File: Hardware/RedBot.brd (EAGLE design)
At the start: 94 x 49.5 mm, 63 parts, among them U1 ATMEGA328P, U2 TB6612FNG, U3 MIC5219 5V, U4 MIC5219 3.3V, U5 FT232RLSSOP, U6 7408SE, Y1 16MHz

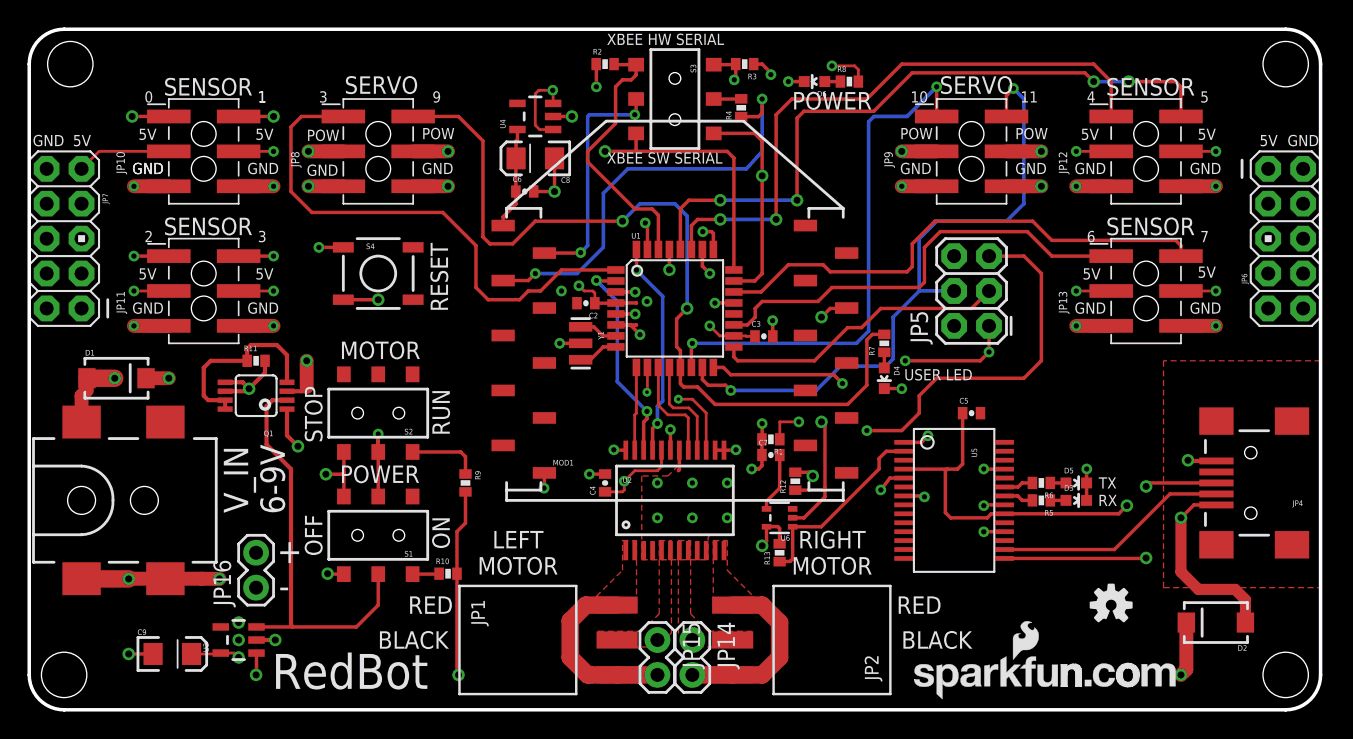
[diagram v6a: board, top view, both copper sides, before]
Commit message: V03 prototypes - Added an AND gate instead of two diodes for reset control - Changed packages on the 5x2 headers along the board edges to be no silk - Moved motor header text to avoid tmask interference - Added bypass cap to FTDI chip - Grounded test pin on FTDI chip
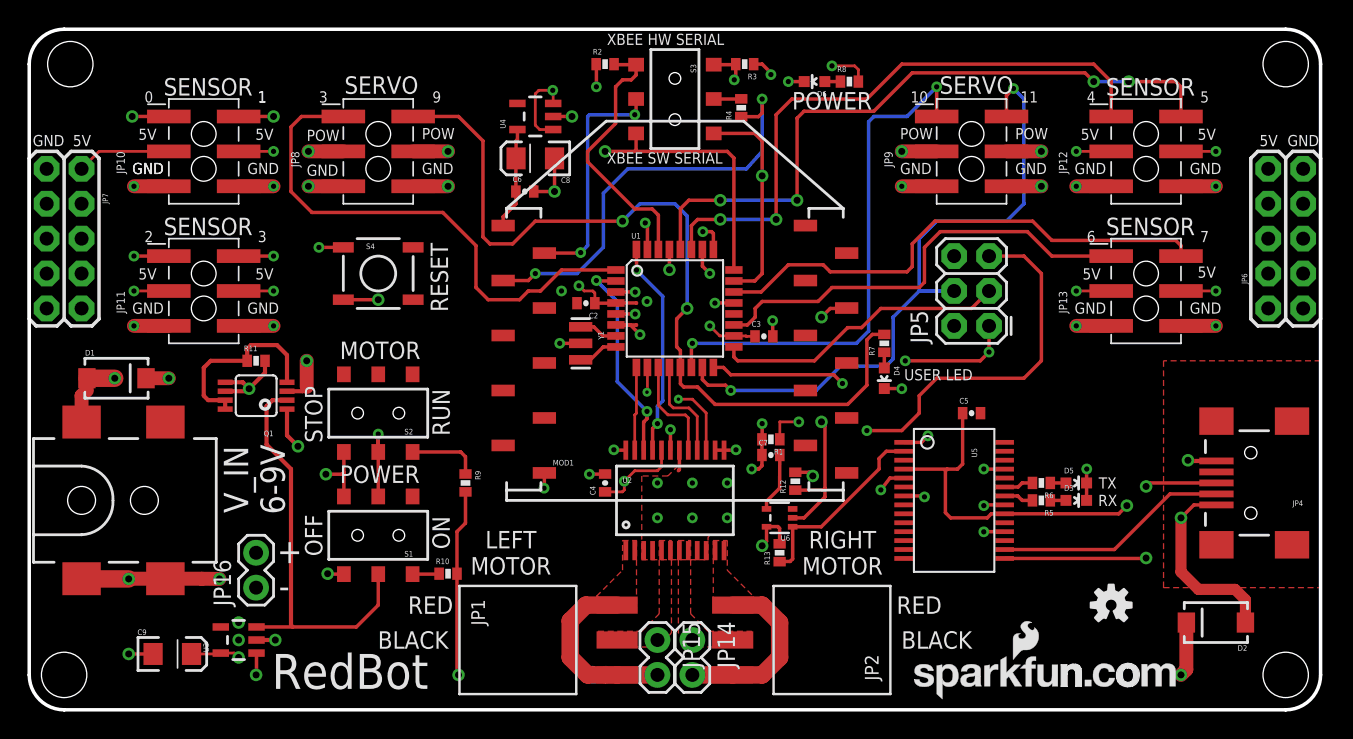
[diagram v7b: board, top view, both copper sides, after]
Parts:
- JP6, JP7: value M05X2PTH -> M05X2NO_SILK; device SparkFun-Connectors:AVR_ICSP -> SparkFun-Connectors:2X5_NOSILK
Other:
- board text added: "v03"
- board text removed: "v10"
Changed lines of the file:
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@@
 <grid distance="0.05" unitdist="inch" unit="inch" style="lines" multiple="1" display="yes" altdistance="0.005" altunitdist="inch" altunit="inch"/>
 <layers>
-<layer number="1" name="Top" color="4" fill="1" visible="yes" active="yes"/>
-<layer number="2" name="5V" color="1" fill="3" visible="yes" active="yes"/>
-<layer number="15" name="Gnd" color="4" fill="6" visible="yes" active="yes"/>
+<layer number="1" name="Top" color="4" fill="1" visible="no" active="yes"/>
+<layer number="2" name="5V" color="1" fill="3" visible="no" active="yes"/>
+<layer number="15" name="Gnd" color="4" fill="6" visible="no" active="yes"/>
 <layer number="16" name="Bottom" color="1" fill="1" visible="yes" active="yes"/>
 <layer number="17" name="Pads" color="2" fill="1" visible="yes" active="yes"/>
@@
 <layer number="19" name="Unrouted" color="6" fill="1" visible="yes" active="yes"/>
 <layer number="20" name="Dimension" color="15" fill="1" visible="yes" active="yes"/>
-<layer number="21" name="tPlace" color="16" fill="1" visible="yes" active="yes"/>
+<layer number="21" name="tPlace" color="16" fill="1" visible="no" active="yes"/>
 <layer number="22" name="bPlace" color="14" fill="1" visible="yes" active="yes"/>
-<layer number="23" name="tOrigins" color="15" fill="1" visible="yes" active="yes"/>
+<layer number="23" name="tOrigins" color="15" fill="1" visible="no" active="yes"/>
 <layer number="24" name="bOrigins" color="15" fill="1" visible="yes" active="yes"/>
 <layer number="25" name="tNames" color="7" fill="1" visible="no" active="yes"/>
@@
 <layer number="42" name="bRestrict" color="1" fill="10" visible="no" active="yes"/>
 <layer number="44" name="Drills" color="7" fill="1" visible="no" active="yes"/>
-<layer number="45" name="Holes" color="7" fill="1" visible="yes" active="yes"/>
+<layer number="45" name="Holes" color="7" fill="1" visible="no" active="yes"/>
 <layer number="46" name="Milling" color="3" fill="1" visible="no" active="yes"/>
-<layer number="51" name="tDocu" color="6" fill="1" visible="yes" active="yes"/>
+<layer number="51" name="tDocu" color="6" fill="1" visible="no" active="yes"/>
 <layer number="52" name="bDocu" color="7" fill="1" visible="no" active="yes"/>
 <layer number="3" name="Route3" color="4" fill="3" visible="no" active="no"/>
@@
 <text x="78.486" y="16.51" size="0.8128" layer="21" font="vector" ratio="15" align="center">TX</text>
 <text x="78.486" y="15.24" size="0.8128" layer="21" font="vector" ratio="15" align="center">RX</text>
-<text x="35.56" y="11.43" size="1.27" layer="21" font="vector" ratio="15" align="center">LEFT
+<text x="35.052" y="11.43" size="1.27" layer="21" font="vector" ratio="15" align="center">LEFT
 MOTOR</text>
-<text x="58.42" y="11.43" size="1.27" layer="21" font="vector" ratio="15" align="center">RIGHT
+<text x="59.182" y="11.43" size="1.27" layer="21" font="vector" ratio="15" align="center">RIGHT
 MOTOR</text>
 <text x="64.77" y="7.62" size="1.27" layer="21" font="vector" ratio="15" align="center">RED</text>
@@
 <text x="58.42" y="44.323" size="1.27" layer="21" font="vector" ratio="15" align="center">POWER</text>
 <text x="66.167" y="24.384" size="0.8128" layer="21" font="vector" ratio="15" align="center">USER LED</text>
-<text x="41.91" y="2.54" size="1.27" layer="16" font="vector" ratio="15" rot="MR0" align="center">v10</text>
+<text x="41.91" y="2.54" size="1.27" layer="16" font="vector" ratio="15" rot="MR0" align="center">v03</text>
 <text x="3.175" y="41.021" size="0.8128" layer="21" font="vector" ratio="15">5V</text>
 <text x="7.493" y="38.989" size="0.8128" layer="21" font="vector" ratio="15">GND</text>
@@
 <text x="18.034" y="10.668" size="1.778" layer="21" font="vector" ratio="15">+</text>
 <text x="18.161" y="8.128" size="1.778" layer="21" font="vector" ratio="15">-</text>
+<wire x1="2.54" y1="40.132" x2="3.048" y2="40.64" width="0.254" layer="21"/>
+<wire x1="3.048" y1="40.64" x2="4.572" y2="40.64" width="0.254" layer="21"/>
+<wire x1="4.572" y1="40.64" x2="5.08" y2="40.132" width="0.254" layer="21"/>
+<wire x1="5.08" y1="40.132" x2="5.08" y2="28.448" width="0.254" layer="21"/>
+<wire x1="5.08" y1="28.448" x2="4.572" y2="27.94" width="0.254" layer="21"/>
+<wire x1="4.572" y1="27.94" x2="3.048" y2="27.94" width="0.254" layer="21"/>
+<wire x1="3.048" y1="27.94" x2="2.54" y2="28.448" width="0.254" layer="21"/>
+<wire x1="2.54" y1="28.448" x2="2.54" y2="40.132" width="0.254" layer="21"/>
+<wire x1="2.54" y1="40.132" x2="2.032" y2="40.64" width="0.254" layer="21"/>
+<wire x1="2.032" y1="40.64" x2="0.508" y2="40.64" width="0.254" layer="21"/>
+<wire x1="0.508" y1="40.64" x2="0" y2="40.132" width="0.254" layer="21"/>
+<wire x1="0" y1="40.132" x2="0" y2="28.448" width="0.254" layer="21"/>
+<wire x1="0" y1="28.448" x2="0.508" y2="27.94" width="0.254" layer="21"/>
+<wire x1="0.508" y1="27.94" x2="2.032" y2="27.94" width="0.254" layer="21"/>
+<wire x1="2.032" y1="27.94" x2="2.54" y2="28.448" width="0.254" layer="21"/>
+<wire x1="91.44" y1="40.132" x2="91.948" y2="40.64" width="0.254" layer="21"/>
+<wire x1="91.948" y1="40.64" x2="93.472" y2="40.64" width="0.254" layer="21"/>
+<wire x1="93.472" y1="40.64" x2="93.98" y2="40.132" width="0.254" layer="21"/>
+<wire x1="93.98" y1="40.132" x2="93.98" y2="28.448" width="0.254" layer="21"/>
+<wire x1="93.98" y1="28.448" x2="93.472" y2="27.94" width="0.254" layer="21"/>
+<wire x1="93.472" y1="27.94" x2="91.948" y2="27.94" width="0.254" layer="21"/>
+<wire x1="91.948" y1="27.94" x2="91.44" y2="28.448" width="0.254" layer="21"/>
+<wire x1="91.44" y1="28.448" x2="91.44" y2="40.132" width="0.254" layer="21"/>
+<wire x1="91.44" y1="40.132" x2="90.932" y2="40.64" width="0.254" layer="21"/>
+<wire x1="90.932" y1="40.64" x2="89.408" y2="40.64" width="0.254" layer="21"/>
+<wire x1="89.408" y1="40.64" x2="88.9" y2="40.132" width="0.254" layer="21"/>
+<wire x1="88.9" y1="40.132" x2="88.9" y2="28.448" width="0.254" layer="21"/>
+<wire x1="88.9" y1="28.448" x2="89.408" y2="27.94" width="0.254" layer="21"/>
+<wire x1="89.408" y1="27.94" x2="90.932" y2="27.94" width="0.254" layer="21"/>
+<wire x1="90.932" y1="27.94" x2="91.44" y2="28.448" width="0.254" layer="21"/>
 </plain>
 <attributes>
@@
 <attribute name="VALUE" value="1k" x="51.816" y="43.815" size="1.778" layer="27" font="vector" ratio="15" rot="R90" display="off"/>
 </element>
-<element name="JP6" library="SparkFun-Connectors" package="AVR_ICSP" value="M05X2PTH" x="91.44" y="34.29"/>
-<element name="JP7" library="SparkFun-Connectors" package="AVR_ICSP" value="M05X2PTH" x="2.54" y="34.29" rot="R180"/>
+<element name="JP6" library="SparkFun-Connectors" package="2X5_NOSILK" value="M05X2NO_SILK" x="91.44" y="34.29"/>
+<element name="JP7" library="SparkFun-Connectors" package="2X5_NOSILK" value="M05X2NO_SILK" x="2.54" y="34.29" rot="R180"/>
 <element name="U$17" library="SparkFun-Aesthetics" package="OSHW-LOGO-S" value="OSHW-LOGOS" x="78.74" y="7.62"/>
 <element name="SFE-LOGO1" library="SparkFun-Aesthetics" package="SFE-NEW-WEBLOGO" value="LOGO-SFENEW" x="64.389" y="0.762"/>
@@
 </element>
 <element name="JP16" library="SparkFun-Connectors" package="1X02" value="" x="16.51" y="8.89" rot="R90"/>
-<element name="U6" library="SparkFun-DigitalIC" package="SOT353" value="7408SE" x="54.61" y="13.97" rot="R90"/>
+<element name="U6" library="SparkFun-DigitalIC" package="SOT353" value="7408SE" x="54.61" y="13.97" rot="R90">
+<attribute name="PROD_ID" value="IC-10841" x="54.61" y="13.97" size="1.778" layer="27" rot="R90" display="off"/>
+<attribute name="VALUE" value="74LVC1G08SE-7" x="54.61" y="13.97" size="1.778" layer="27" rot="R90" display="off"/>
+</element>
 <element name="R12" library="SparkFun-Resistors" package="0402-RES" value="10k" x="55.753" y="16.637" rot="R90">
 <attribute name="PROD_ID" value="RES-00824" x="55.753" y="16.637" size="1.778" layer="27" font="vector" ratio="15" rot="R90" display="off"/>
@@
 </signal>
 </signals>
-<errors>
-</errors>
 </board>
 </drawing>

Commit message: Change board/schematic to v10  - Tweaks to board labels  - Change as many 0.015" vias to 0.020" as possible.  - Address a few minor clearance issues.
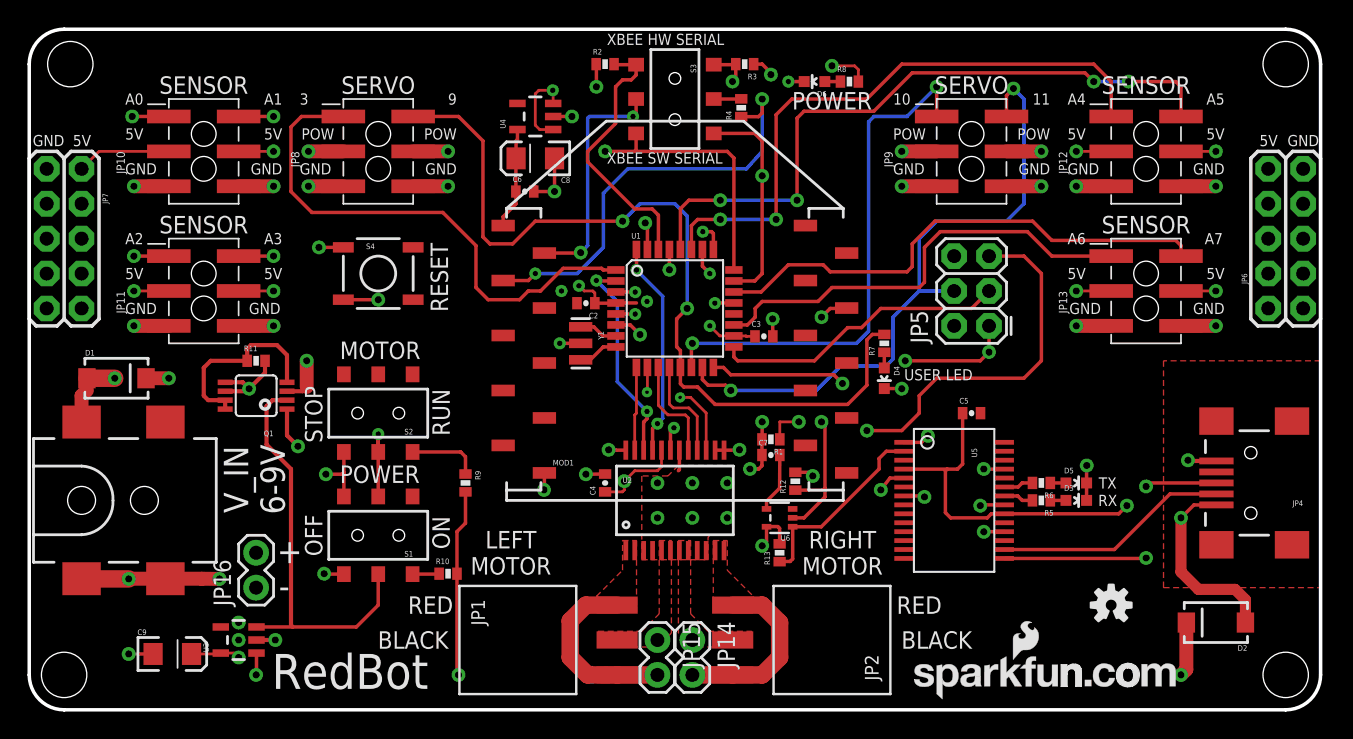
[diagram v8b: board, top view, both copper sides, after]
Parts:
- added U$21: FOUR_LAYER_WARNING, SparkFun-Aesthetics:FOUR_LAYER_WARNING
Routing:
- net 5V: track 63.7 -> 62.1 mm
- net GND: track 83.5 -> 84.7 mm
- net V_BATT: track 79.9 -> 80.8 mm
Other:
- board text added: "A0"
- board text added: "A1"
- board text added: "A2"
- board text added: "A3"
- board text added: "A4"
- board text added: "A5"
- board text added: "A6"
- board text added: "A7"
- board text added: "sparkfun.com/redbot"
- board text added: "v10"
- board text removed: "0"
- board text removed: "1"
- board text removed: "2"
- board text removed: "4"
- board text removed: "5"
- board text removed: "6"
- board text removed: "7"
- board text removed: "v03"
